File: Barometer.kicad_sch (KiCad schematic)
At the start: 6 parts, among them J19 Conn_01x02, U3 BMP280

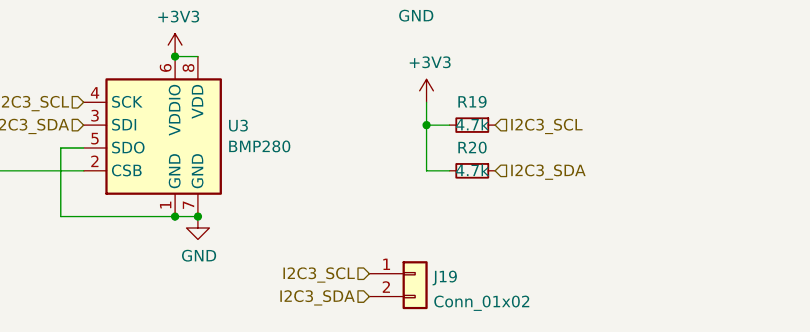
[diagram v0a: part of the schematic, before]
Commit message: Finished power and signal routing.
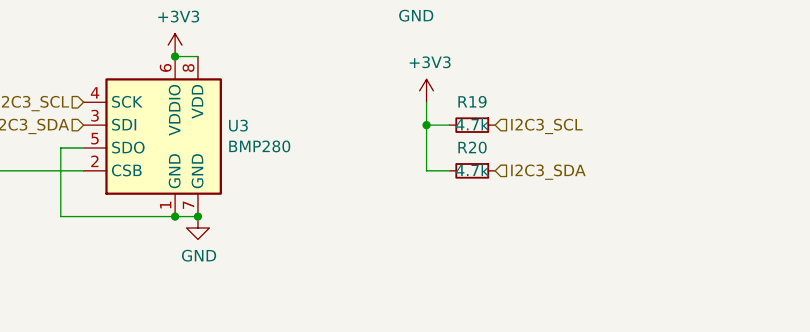
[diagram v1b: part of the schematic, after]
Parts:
- removed J19: Conn_01x02, MyConnectors:I2C_Probe, symbol Connector_Generic:Conn_01x02
